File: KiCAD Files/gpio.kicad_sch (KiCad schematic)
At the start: 4 parts, among them J1 REV_JST_SMD, J2 REV_JST_SMD, U1 K230_Rewired

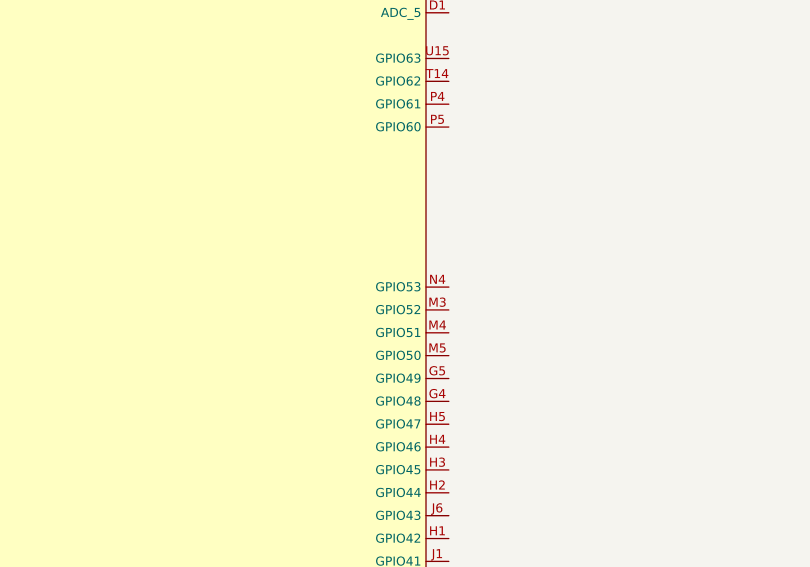
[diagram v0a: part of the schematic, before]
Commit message: added ram and flash
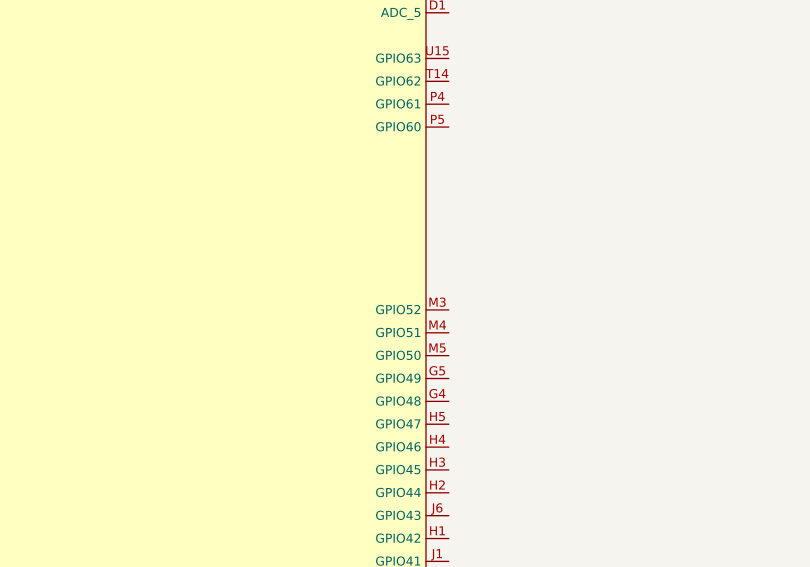
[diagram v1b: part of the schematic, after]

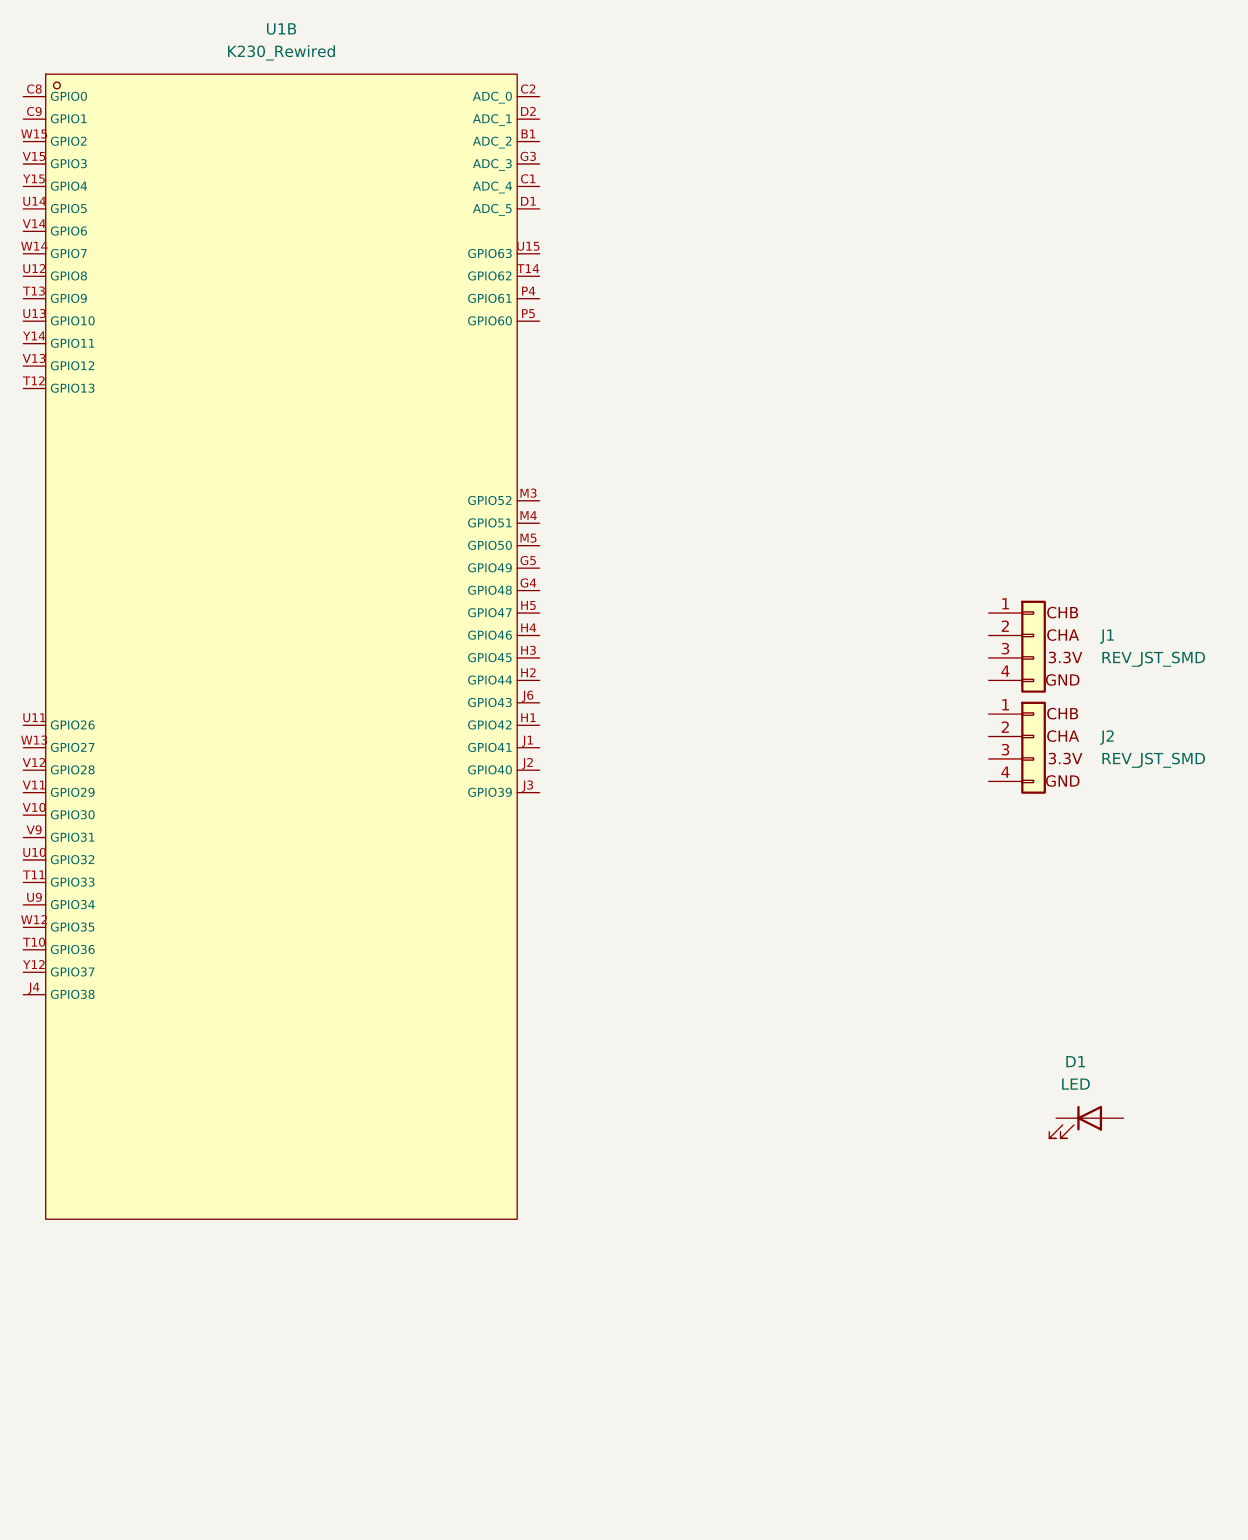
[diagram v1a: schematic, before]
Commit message: more peripherals
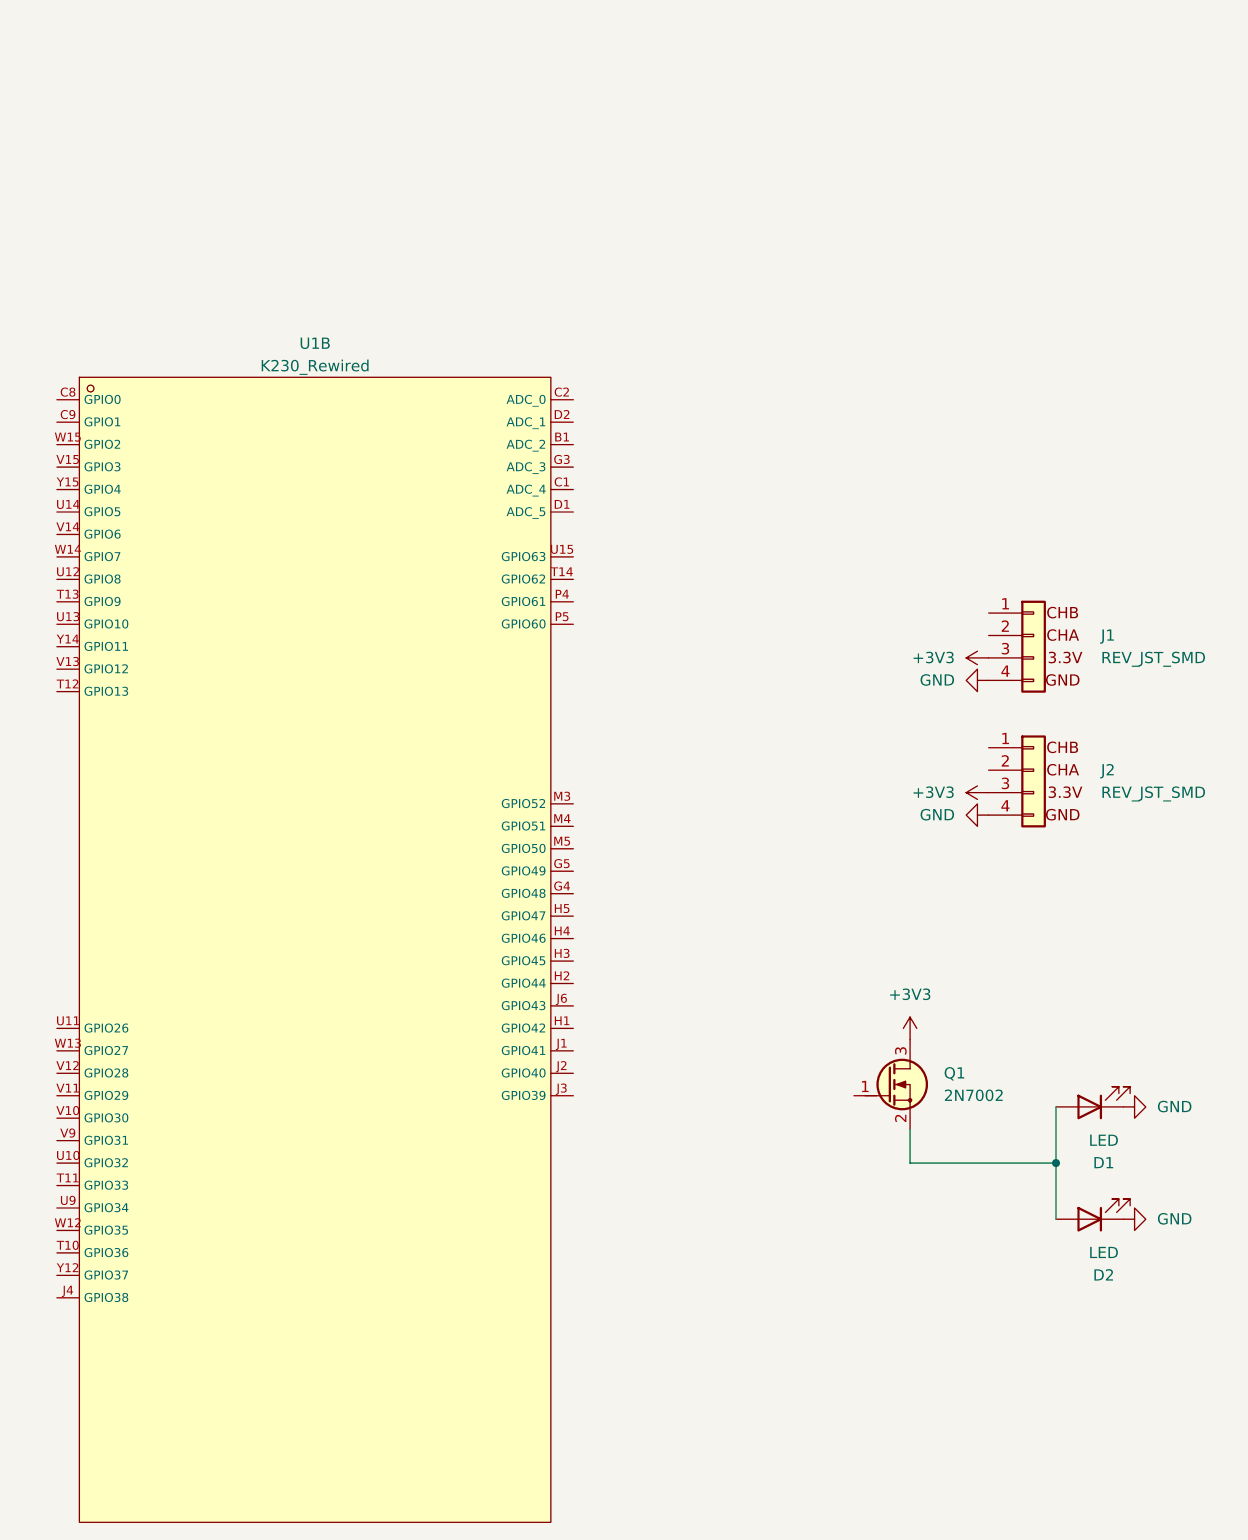
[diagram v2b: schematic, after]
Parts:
- added D2: LED, LED_SMD:LED_PLCC_2835, symbol Device:LED
- added Q1: 2N7002, PCM_Package_TO_SOT_SMD_AKL:SOT-23, symbol PCM_Transistor_MOSFET_AKL:2N7002
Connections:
- net +3V3: now reaches J1.3 (3.3V)
- net +3V3: now also J2.3 (3.3V), Q1.3 (D)
- net GND: now reaches J1.4 (GND)
- net GND: now also D1.1 (K), J2.4 (GND), D2.1 (K)
- net at D1.2 (A): now also D2.2 (A), Q1.2 (S)
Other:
- moved on the sheet: D1, J2, U1B
